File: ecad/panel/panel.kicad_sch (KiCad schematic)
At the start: 208 parts, among them J2 Conn_01x03_Pin, J3 USB4105-GF-A, J4 5017868090, SW1 SW_SPDT, SW10 SW_SPDT, SW11 SW_SPDT, SW12 SW_SPDT, SW13 SW_SPDT, SW14 SW_SPDT, SW15 SW_SPDT, SW16 SW_SPDT, SW17 SW_Push, SW18 SW_Push, SW19 SW_Push, SW2 SW_SPDT, SW20 SW_Push, SW21 SW_Push, SW22 SW_Push, SW23 SW_Push, SW24 SW_Push, SW25 SW_Push, SW26 SW_Push, SW27 SW_Push, SW28 SW_Push, SW29 SW_Push, SW3 SW_SPDT, SW30 SW_Push, SW4 SW_SPDT, SW5 SW_SPDT, SW6 SW_SPDT, SW7 SW_SPDT, SW8 SW_SPDT, SW9 SW_SPDT, U1 TLC59211IN, U10 NCP1117-3.3_SOT223, U2 TLC59211IN, U3 TLC59211IN, U4 TLC59211IN, U5 TLC59211IN, U6 RP2350_80QFN, U7 W25Q128JVS, U8 MCP23017_SO, U9 MCP23017_SO, X1 ABM8-272-T3

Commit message: near-final panel routing
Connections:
- net I2C0_SCK is gone; now on net I2C1_SCK: U8.12 (SCK)
- net I2C0_SDA is gone; now on net I2C1_SDA: U8.13 (SDA)
- net A0_LED: now also U5.16 (*Y4); no longer U5.19 (*Y1)
- net A10: now also R86.2; no longer R53.2
- net A10_LED: now also U3.16 (*Y4); no longer U3.17 (*Y3)
- net A10_SW: now also U9.26 (GPA5); no longer U8.6 (GPB5)
- net A11: now also R80.2; no longer R51.2
- net A11_LED: now also U3.14 (*Y6); no longer U3.16 (*Y4)
- net A11_SW: now also U9.25 (GPA4); no longer U8.5 (GPB4)
- net A12: now also R53.2; no longer R79.2
- net A12_LED: now also U2.19 (*Y1); no longer U3.15 (*Y5)
- net A12_SW: now also U9.24 (GPA3); no longer U8.4 (GPB3)
- net A13: now also R51.2; no longer R80.2
- net A13_LED: now also U2.18 (*Y2); no longer U3.14 (*Y6)
- net A13_SW: now also U9.23 (GPA2); no longer U8.3 (GPB2)
- net A14: now also R48.2; no longer R45.2
- net A14_LED: now also U2.15 (*Y5); no longer U3.13 (*Y7)
- net A14_SW: now also U9.22 (GPA1); no longer U8.2 (GPB1)
- net A15: now also R45.2; no longer R48.2
- net A15_LED: now also U2.12 (*Y8); no longer U3.12 (*Y8)
- net A15_SW: now also U9.21 (GPA0); no longer U8.1 (GPB0)
- net A1_LED: now also U5.17 (*Y3); no longer U5.18 (*Y2)
- net A2_LED: now also U5.14 (*Y6); no longer U5.17 (*Y3)
- net A3: now also J4.3
- net A3_LED: now also U5.12 (*Y8); no longer U5.16 (*Y4)
- net A4: now also J4.47, R57.2; no longer J4.44, R64.2
- net A4_LED: now also U4.19 (*Y1); no longer U5.15 (*Y5)
- net A5: now also J4.45, R59.2; no longer J4.46, R63.2
- net A5_LED: now also U4.17 (*Y3); no longer U5.14 (*Y6)
- net A6: now also R63.2; no longer R59.2
- net A6_LED: now also U4.14 (*Y6); no longer U5.13 (*Y7)
- net A7: now also R61.2; no longer R60.2
- net A7_LED: now also U4.15 (*Y5); no longer U5.12 (*Y8)
- net A8: now also R83.2; no longer R56.2
- net A8_SW: now also U9.28 (GPA7); no longer U8.8 (GPB7)
- net A9: now also R84.2; no longer R55.2
- net A9_SW: now also U9.27 (GPA6); no longer U8.7 (GPB6)
- net AUX1: now also U8.3 (GPB2); no longer U9.22 (GPA1)
- net AUX2: now also U8.5 (GPB4); no longer U9.21 (GPA0)
- net CLR: now also U8.1 (GPB0); no longer U9.25 (GPA4)
- net D0_LED: now also U5.19 (*Y1); no longer U4.19 (*Y1)
- net D1_LED: now also U5.18 (*Y2); no longer U4.18 (*Y2)
- net D2_LED: now also U5.15 (*Y5); no longer U4.17 (*Y3)
- net D3_LED: now also U5.13 (*Y7); no longer U4.16 (*Y4)
- net D4: now also J4.46, R58.2; no longer J4.45, R62.2
- net D4_LED: now also U4.18 (*Y2); no longer U4.15 (*Y5)
- net D5: now also J4.44, R60.2; no longer J4.47, R61.2
- net D5_LED: now also U4.16 (*Y4); no longer U4.14 (*Y6)
- net D6: now also R62.2; no longer R58.2
- net D7: now also R64.2; no longer R57.2
- net DEPOSIT: now also U8.28 (GPA7); no longer U8.21 (GPA0)
- net DEPOSIT_NEXT: now also U8.26 (GPA5); no longer U8.22 (GPA1)
- net EXAMINE: now also U8.25 (GPA4); no longer U8.23 (GPA2)
- net HDLA_LED: now also U1.12 (*Y8); no longer U1.15 (*Y5)
- net HLDA: now also R52.2; no longer R86.2
- net HLTA: now also R77.2; no longer R49.2
- net HLTA_LED: now also U3.12 (*Y8); no longer U2.16 (*Y4)
- net INP: now also R46.2; no longer R47.2
- net INT: now also R85.2; no longer R54.2
- net INTE: now also R55.2; no longer R84.2
- net INTE_LED: now also U1.14 (*Y6); no longer U1.13 (*Y7)
- net INT_LED: now also U3.17 (*Y3); no longer U2.19 (*Y1)
- net M1: now also R49.2; no longer R77.2
- net MEMR: now also R47.2; no longer R46.2
- net MEMR_LED: now also U2.14 (*Y6); no longer U2.12 (*Y8)
- net OUT: now also R50.2; no longer R78.2
- net OUT_LED: now also U2.17 (*Y3); no longer U2.15 (*Y5)
- net PROT: now also R56.2; no longer R83.2
- net PROTECT: now also U8.4 (GPB3); no longer U9.24 (GPA3)
- net PROT_LED: now also U1.15 (*Y5); no longer U1.12 (*Y8)
- net RESET: now also U8.27 (GPA6); no longer U9.26 (GPA5)
- net RUN: now also U8.21 (GPA0); no longer U8.27 (GPA6)
- net SINGLE_STEP: now also U8.23 (GPA2); no longer U8.25 (GPA4)
- net STACK: now also R78.2; no longer R50.2
- net STACK_LED: now also U3.13 (*Y7); no longer U2.17 (*Y3)
- net STOP: now also U8.22 (GPA1); no longer U8.28 (GPA7)
- net UNPROTECT: now also U8.2 (GPB1); no longer U9.23 (GPA2)
- net WAIT: now also R54.2; no longer R85.2
- net WAIT_LED: now also U1.13 (*Y7); no longer U1.14 (*Y6)
- net WO: now also R79.2; no longer R52.2
- net WO_LED: now also U3.15 (*Y5); no longer U2.18 (*Y2)
- net PUSH_INTB: now reaches U8.19 (INTB)
- net PUSH_INTA: now reaches U8.20 (INTA)
- net MI_LED renamed M1_LED
- net M1_LED: now also U2.16 (*Y4); no longer U2.14 (*Y6)
- no-connect marks 117 -> 114

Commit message: minor panel adj.
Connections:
- net PUSH_INTA: now also U6.45 (GPIO36)
- net PUSH_INTB: now also U6.46 (GPIO37)
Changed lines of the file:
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@@
 	(wire
 		(pts
-			(xy 199.39 175.26) (xy 220.98 175.26)
-		)
-		(stroke
-			(width 0)
-			(type default)
-		)
-	)
-	(wire
-		(pts
 			(xy 243.84 350.52) (xy 246.38 350.52)
 		)
@@
 	(wire
 		(pts
-			(xy 199.39 177.8) (xy 220.98 177.8)
-		)
-		(stroke
-			(width 0)
-			(type default)
-		)
-	)
-	(wire
-		(pts
 			(xy 298.45 201.93) (xy 298.45 204.47)
 		)
@@
 	(wire
 		(pts
+			(xy 199.39 177.8) (xy 218.44 177.8)
+		)
+		(stroke
+			(width 0)
+			(type default)
+		)
+	)
+	(wire
+		(pts
 			(xy 417.83 36.83) (xy 427.99 36.83)
 		)
@@
 	(wire
 		(pts
+			(xy 199.39 175.26) (xy 218.44 175.26)
+		)
+		(stroke
+			(width 0)
+			(type default)
+		)
+	)
+	(wire
+		(pts
 			(xy 111.76 172.72) (xy 111.76 165.1)
 		)
@@
 		)
 	)
+	(label "PUSH_INTB"
+		(at 218.44 177.8 180)
+		(effects
+			(font
+				(size 1.27 1.27)
+			)
+			(justify right bottom)
+		)
+	)
 	(label "BUS71"
 		(at 417.83 102.87 180)
@@
 			)
 			(justify right bottom)
+		)
+	)
+	(label "PUSH_INTA"
+		(at 218.44 175.26 180)
+		(effects
+			(font
+				(size 1.27 1.27)
+			)
+			(justify right bottom)

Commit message: panel, routing, USB, switches, LDO
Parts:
- added R90: 1k, Resistor_SMD:R_0402_1005Metric_Pad0.72x0.64mm_HandSolder, symbol Device:R
- added SW31: SW_Push, Button_Switch_SMD:SW_Push_1P1T_NO_Vertical_Wuerth_434133025816, symbol Switch:SW_Push
- J3: value USB4105-GF-A -> USB4235-03-C; footprint Library:GCT_USB4105-GF-A -> Library:GCT_USB4235-03-C_REVA; symbol Project_Library:USB4105-GF-A -> Project_Library:USB4235-03-C_REVA; Availability (none) -> In Stock; Check_prices (none) -> https://www.snapeda.com/parts/USB4235-03-C/Global+Connector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; Description_1 (none) -> USB-C (USB TYPE-C) USB 2.0 Receptacle Connector 24 (16+8 Du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; MANUFACTURER GCT -> Global Connector Technology; MAXIMUM_PACKAGE_HEIGHT 3.31 mm -> 6.5mm; MF (none) -> Global Connector Technology; MP (none) -> USB4235-03-C; PARTREV B4 -> A; Package (none) -> None; Price (none) -> None; SnapEDA_Link (none) -> https://www.snapeda.com/parts/USB4235-03-C/Global+Connector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
- SW30: footprint Library:SW_1825910-6-4 -> Button_Switch_SMD:SW_Push_1P1T_NO_Vertical_Wuerth_434133025816
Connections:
- net GND: now also J3.A1 (GND_A), J3.A12 (GND_A), J3.B1 (GND_B), J3.B12 (GND_B), SW31.1; no longer J3.A1_B12 (GND), J3.B1_A12 (GND__1), J3.SH3 (SHELL_GND__2), J3.SH4 (SHELL_GND__3)
- net USB_D+: now also J3.B6 (DP2); no longer J3.A5 (CC1)
- net VBUS: now also J3.A4 (VBUS_A), J3.A9 (VBUS_A), J3.B4 (VBUS_B), J3.B9 (VBUS_B); no longer D37.2 (A), D40.2 (A), J3.A4_B9 (VBUS), J3.B4_A9 (VBUS__1)
- net at R29.2: now also J3.A5 (CC1); no longer J3.B5 (CC2)
- net at R30.2: now also J3.B5 (CC2); no longer J3.B6 (DP2)
- net at U6.75 (QSPI_SS), U7.1 (~{CS}): now also R90.2
- new net ~{USB_BOOT}: R90.1, SW31.2
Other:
- moved on the sheet: D37, D40, R29, R30, R89

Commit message: Changes
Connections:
- net GND: no longer SW1.3 (C), SW10.3 (C), SW11.3 (C), SW12.3 (C), SW13.3 (C), SW14.3 (C), SW15.3 (C), SW16.3 (C), SW2.3 (C), SW3.3 (C), SW4.3 (C), SW5.3 (C), SW6.3 (C), SW7.3 (C), SW8.3 (C), SW9.3 (C)
- no-connect marks 114 -> 130
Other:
- moved on the sheet: SW20, SW21, SW22, SW23, SW24, SW25, SW26, SW27, SW28, SW29

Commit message: more panel work
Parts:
- removed D40: D_Schottky, symbol Device:D_Schottky
- R1, R10, R11, R12, R13, R14, R15, R16, R17, R18, R19, R2, R20, R21, R22, R23, R24, R3, R33, R34, R35, R36, R37, R38, R39, R4, R40, R41, R42, R43, R44, R5, R6, R7, R8, R9: value 470 -> 68
- R89: value R -> 150
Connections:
- net 3.3V: now also C29.1, D41.2 (A), U10.2 (VO); no longer D41.1 (K)
- net VBUS: now also D41.1 (K)
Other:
- moved on the sheet: D41

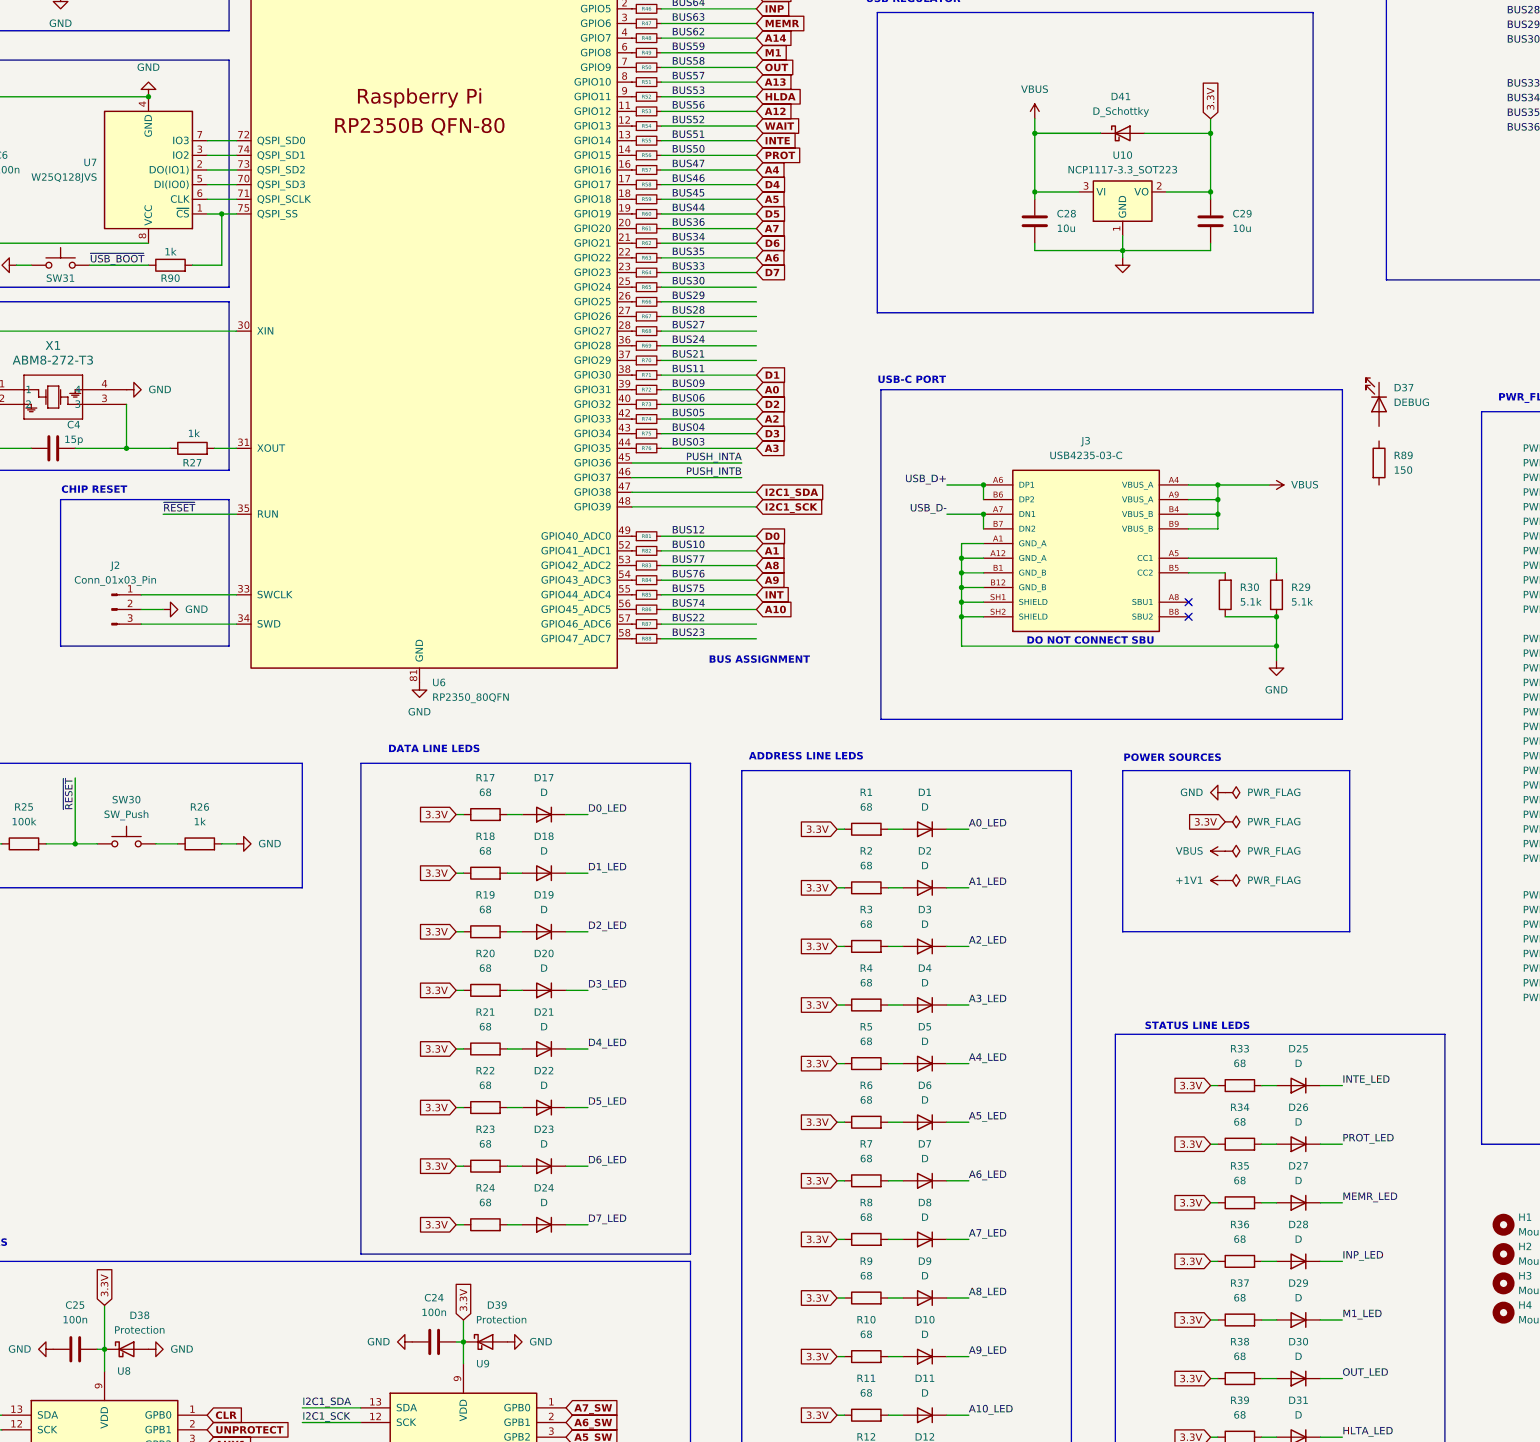
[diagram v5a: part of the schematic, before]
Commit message: new diode, some panel pwr routing
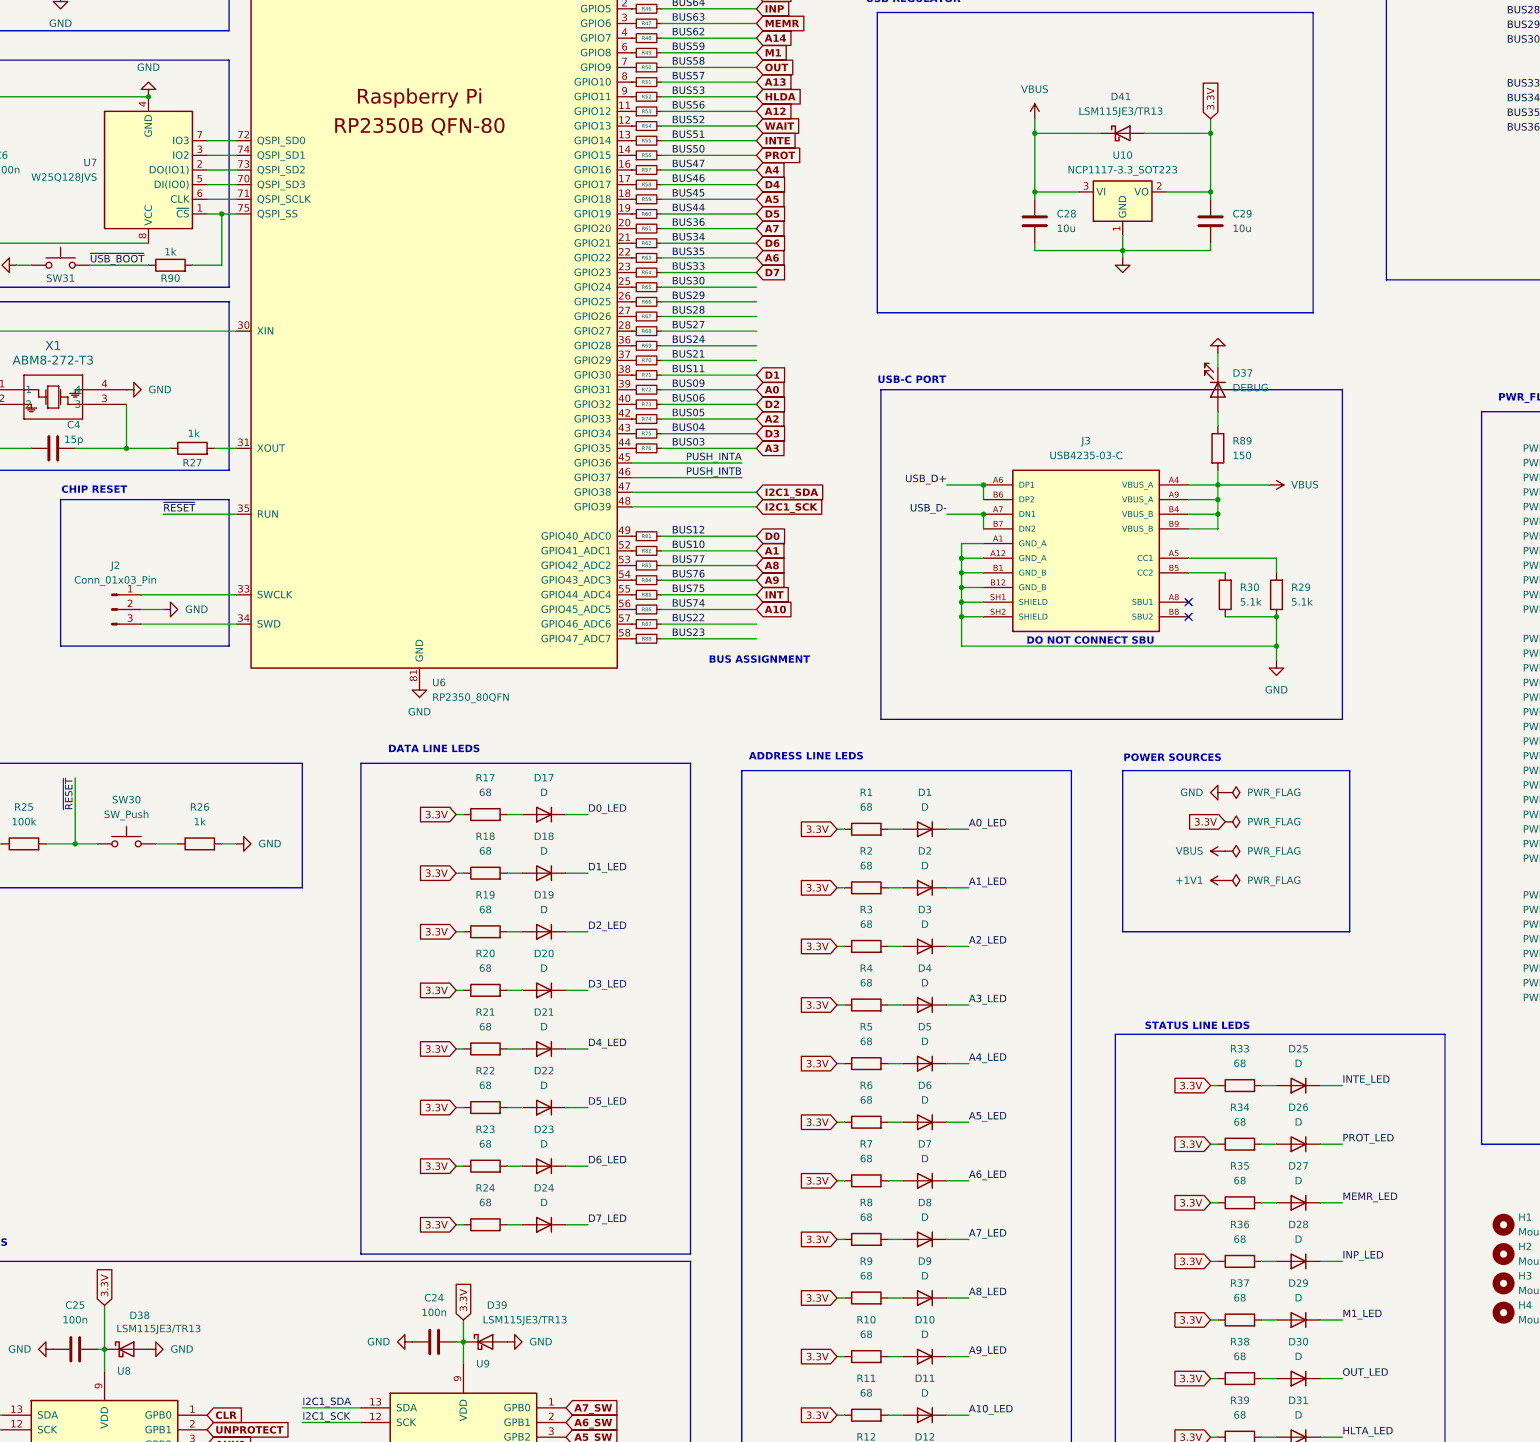
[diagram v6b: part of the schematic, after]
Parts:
- D37: footprint Diode_SMD:D_0402_1005Metric_Pad0.77x0.64mm_HandSolder -> LED_SMD:LED_0603_1608Metric_Pad1.05x0.95mm_HandSolder
- D38, D39: value Protection -> LSM115JE3/TR13; footprint (none) -> Library:DO-214BA_MCH-L
- D41: value D_Schottky -> LSM115JE3/TR13; footprint Diode_SMD:D_0402_1005Metric -> Library:DO-214BA_MCH-L
- R89: footprint (none) -> Resistor_SMD:R_0402_1005Metric_Pad0.72x0.64mm_HandSolder
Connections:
- net GND: now also D37.1 (K)
- net VBUS: now also R89.2
- net at R89.1: now also D37.2 (A)
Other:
- moved on the sheet: D37, R89
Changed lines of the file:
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@@
 	(wire
 		(pts
-			(xy 269.24 118.11) (xy 280.67 118.11)
-		)
-		(stroke
-			(width 0)
-			(type default)
-		)
-	)
-	(wire
-		(pts
 			(xy 27.94 384.81) (xy 31.75 384.81)
 		)
@@
 	(wire
 		(pts
+			(xy 300.99 156.21) (xy 300.99 158.75)
+		)
+		(stroke
+			(width 0)
+			(type default)
+		)
+	)
+	(wire
+		(pts
 			(xy 417.83 41.91) (xy 427.99 41.91)
 		)
@@
 	(wire
 		(pts
+			(xy 300.99 166.37) (xy 300.99 168.91)
+		)
+		(stroke
+			(width 0)
+			(type default)
+		)
+	)
+	(wire
+		(pts
 			(xy 80.01 340.36) (xy 90.17 340.36)
 		)
@@
 	(wire
 		(pts
+			(xy 300.99 176.53) (xy 300.99 179.07)
+		)
+		(stroke
+			(width 0)
+			(type default)
+		)
+	)
+	(wire
+		(pts
 			(xy 356.87 52.07) (xy 367.03 52.07)
 		)
@@
 			)
 		)
-		(property "Value" "D_Schottky"
+		(property "Value" "LSM115JE3/TR13"
 			(at 284.1625 114.3 0)
 			(effects
@@
 			)
 		)
-		(property "Footprint" "Diode_SMD:D_0402_1005Metric"
+		(property "Footprint" "Library:DO-214BA_MCH-L"
 			(at 284.48 118.11 0)
 			(effects
@@
 			)
 		)
-		(property "Value" "Protection"
-			(at 176.784 323.85 0)
+		(property "Value" "LSM115JE3/TR13"
+			(at 180.848 323.85 0)
 			(effects
 				(font
@@
 			)
 		)
-		(property "Footprint" ""
+		(property "Footprint" "Library:DO-214BA_MCH-L"
 			(at 173.99 327.66 0)
 			(effects
@@
 	)
 	(symbol
+		(lib_id "power:GND")
+		(at 300.99 156.21 180)
+		(unit 1)
+		(exclude_from_sim no)
+		(in_bom yes)
+		(on_board yes)
+		(dnp no)
+		(fields_autoplaced yes)
+		(property "Reference" "#PWR01"
+			(at 300.99 149.86 0)
+			(effects
+				(font
+					(size 1.27 1.27)
+				)
+				(hide yes)
+			)
+		)
+		(property "Value" "GND"
+			(at 300.99 151.13 0)
+			(effects
+				(font
+					(size 1.27 1.27)
+				)
+				(hide yes)
+			)
+		)
+		(property "Footprint" ""
+			(at 300.99 156.21 0)
+			(effects
+				(font
+					(size 1.27 1.27)
+				)
+				(hide yes)
+			)
+		)
+		(property "Datasheet" ""
+			(at 300.99 156.21 0)
+			(effects
+				(font
+					(size 1.27 1.27)
+				)
+				(hide yes)
+			)
+		)
+		(property "Description" "Power symbol creates a global label with name \"GND\" , ground"
+			(at 300.99 156.21 0)
+			(effects
+				(font
+					(size 1.27 1.27)
+				)
+				(hide yes)
+			)
+		)
+		(pin "1"
+		)
+		(instances
+			(project "panel"
+				(path "/53fb923b-a98b-45c5-8e11-289a5d1ad382"
+					(reference "#PWR01")
+					(unit 1)
+				)
+			)
+		)
+	)
+	(symbol
 		(lib_id "Device:C")
 		(at 181.61 39.37 0)
@@
 	(symbol
 		(lib_id "Device:R")
-		(at 328.93 175.26 0)
+		(at 300.99 172.72 0)
 		(unit 1)
 		(exclude_from_sim no)
@@
 		(fields_autoplaced yes)
 		(property "Reference" "R89"
-			(at 331.47 173.9899 0)
+			(at 303.53 171.4499 0)
 			(effects
 				(font
@@
 		)
 		(property "Value" "150"
-			(at 331.47 176.5299 0)
+			(at 303.53 173.9899 0)
 			(effects
 				(font
@@
 			)
 		)
-		(property "Footprint" ""
-			(at 327.152 175.26 90)
+		(property "Footprint" "Resistor_SMD:R_0402_1005Metric_Pad0.72x0.64mm_HandSolder"
+			(at 299.212 172.72 90)
 			(effects
 				(font
@@
 		)
 		(property "Datasheet" "~"
-			(at 328.93 175.26 0)
+			(at 300.99 172.72 0)
 			(effects
 				(font
@@
 		)
 		(property "Description" "Resistor"
-			(at 328.93 175.26 0)
+			(at 300.99 172.72 0)
 			(effects
 				(font
@@
 	(symbol
 		(lib_id "Device:LED")
-		(at 328.93 165.1 270)
+		(at 300.99 162.56 270)
 		(unit 1)
 		(exclude_from_sim no)
@@
 		(fields_autoplaced yes)
 		(property "Reference" "D37"
-			(at 331.47 162.2424 90)
+			(at 303.53 159.7024 90)
 			(effects
 				(font
@@
 		)
 		(property "Value" "DEBUG"
-			(at 331.47 164.7824 90)
+			(at 303.53 162.2424 90)
 			(effects
 				(font
@@
 			)
 		)
-		(property "Footprint" "Diode_SMD:D_0402_1005Metric_Pad0.77x0.64mm_HandSolder"
-			(at 328.93 165.1 0)
+		(property "Footprint" "LED_SMD:LED_0603_1608Metric_Pad1.05x0.95mm_HandSolder"
+			(at 300.99 162.56 0)
 			(effects
 				(font
@@
 		)
 		(property "Datasheet" "~"
-			(at 328.93 165.1 0)
+			(at 300.99 162.56 0)
 			(effects
 				(font
@@
 		)
 		(property "Description" "Light emitting diode"
-			(at 328.93 165.1 0)
+			(at 300.99 162.56 0)
 			(effects
 				(font
@@
 			)
 		)
-		(property "Value" "Protection"
-			(at 114.046 325.628 0)
+		(property "Value" "LSM115JE3/TR13"
+			(at 117.348 325.374 0)
 			(effects
 				(font
@@
 			)
 		)
-		(property "Footprint" ""
+		(property "Footprint" "Library:DO-214BA_MCH-L"
 			(at 111.76 328.93 0)
 			(effects

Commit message: Panel final? route
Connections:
- net 3.3V: now also U6.15 (IOVDD), U6.24 (IOVDD), U6.29 (IOVDD), U6.41 (IOVDD), U6.5 (IOVDD), U6.50 (IOVDD), U6.59 (ADC_AVDD), U6.60 (IOVDD), U6.68 (USB_OTP_VDD), U6.69 (QSPI_IOVDD), U6.76 (IOVDD)
- net GND: no longer U6.15 (IOVDD), U6.24 (IOVDD), U6.29 (IOVDD), U6.41 (IOVDD), U6.5 (IOVDD), U6.50 (IOVDD), U6.59 (ADC_AVDD), U6.60 (IOVDD), U6.68 (USB_OTP_VDD), U6.69 (QSPI_IOVDD), U6.76 (IOVDD)
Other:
- moved on the sheet: C13, C14, C15, C16, C17, C18, C19, C20, C21, C22, C23
